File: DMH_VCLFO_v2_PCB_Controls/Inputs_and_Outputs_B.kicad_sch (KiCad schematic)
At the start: 41 parts, among them J13 TS_Jack_6.35mm_Sw, J14 TS_Jack_6.35mm_Sw, J15 TS_Jack_6.35mm_Sw, J16 TS_Jack_6.35mm_Sw, J17 TS_Jack_6.35mm_Sw, J18 TS_Jack_6.35mm_Sw, J29 Conn_01x08, J30 Conn_01x08, J31 IDC_02x05, J32 Conn_01x08, J33 Conn_01x08, Q5 BC548, Q6 BC558, SW10 SPDT_OnOffOn, SW11 SW_SPDT, SW12 SW_SPDT, SW9 SW_SPDT, U3 TL074

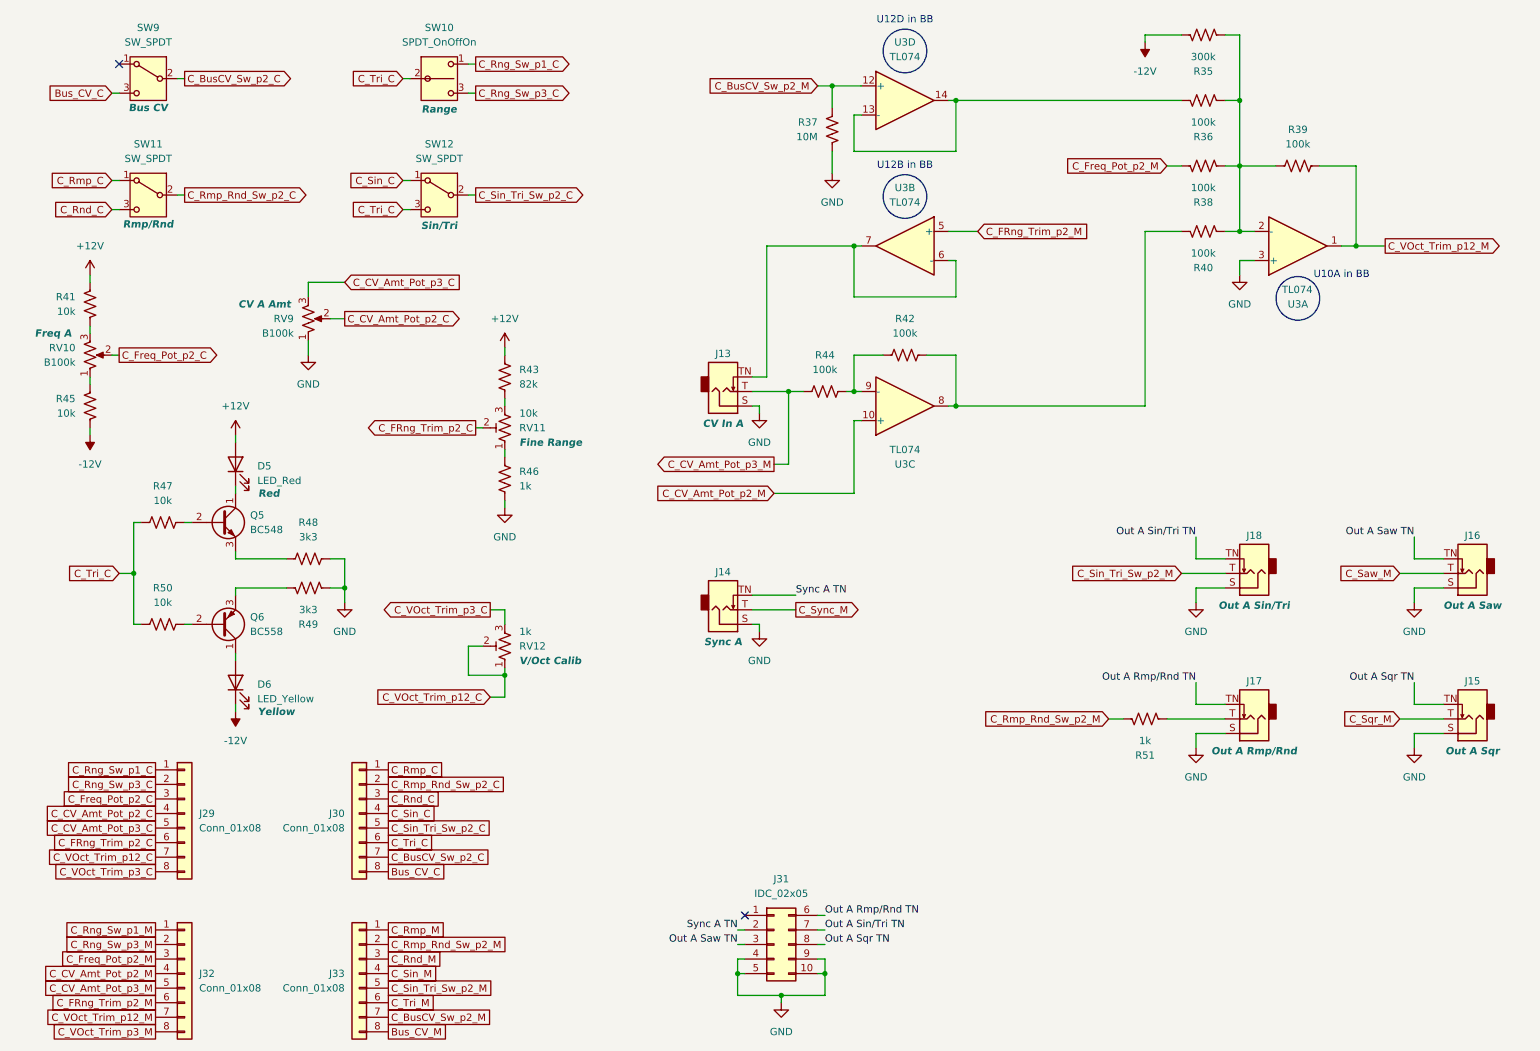
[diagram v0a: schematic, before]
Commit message: Controls PCB comp placement in progress
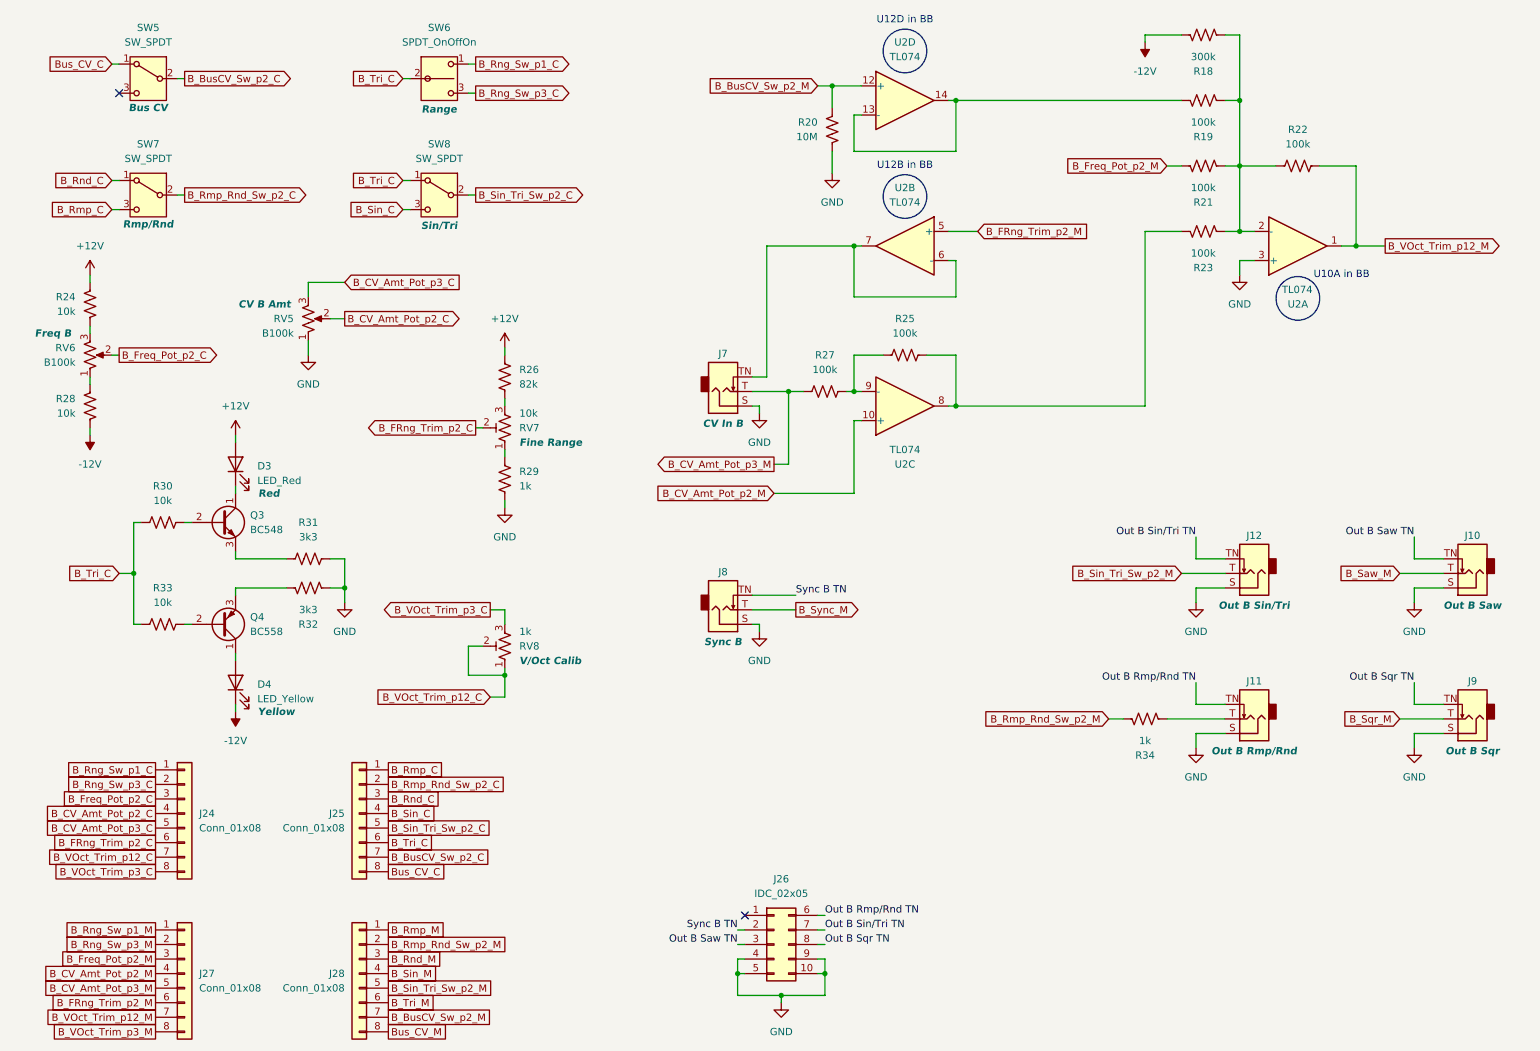
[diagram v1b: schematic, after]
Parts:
- J10: renamed from J16; Function Out A Saw -> Out B Saw
- J11: renamed from J17; Function Out A Rmp/Rnd -> Out B Rmp/Rnd
- J12: renamed from J18; Function Out A Sin/Tri -> Out B Sin/Tri
- J24: renamed from J29; footprint Connector_PinHeader_2.54mm:PinHeader_1x08_P2.54mm_Vertical -> Connector_PinSocket_2.54mm:PinSocket_1x08_P2.54mm_Vertical
- J25: renamed from J30; footprint Connector_PinHeader_2.54mm:PinHeader_1x08_P2.54mm_Vertical -> Connector_PinSocket_2.54mm:PinSocket_1x08_P2.54mm_Vertical
- J7: renamed from J13; Function CV In A -> CV In B
- J8: renamed from J14; Function Sync A -> Sync B
- J9: renamed from J15; Function Out A Sqr -> Out B Sqr
- RV5: renamed from RV9; Function CV A Amt -> CV B Amt
- RV6: renamed from RV10; Function Freq A -> Freq B
- renumbered D5 to D3, D6 to D4, J31 to J26, J32 to J27, J33 to J28, Q5 to Q3, Q6 to Q4, R35 to R18, R36 to R19, R37 to R20, R38 to R21, R39 to R22, R40 to R23, R41 to R24, R42 to R25, R43 to R26, R44 to R27, R45 to R28, R46 to R29, R47 to R30, R48 to R31, R49 to R32, R50 to R33, R51 to R34, RV11 to RV7, RV12 to RV8, SW9 to SW5, SW10 to SW6, SW11 to SW7, SW12 to SW8, U3 to U2
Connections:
- net Bus_CV_C: now also SW5.1 (A); no longer SW5.3 (C)
- net C_BusCV_Sw_p2_C renamed B_BusCV_Sw_p2_C
- net C_BusCV_Sw_p2_M renamed B_BusCV_Sw_p2_M
- net C_CV_Amt_Pot_p2_C renamed B_CV_Amt_Pot_p2_C
- net C_CV_Amt_Pot_p2_M renamed B_CV_Amt_Pot_p2_M
- net C_CV_Amt_Pot_p3_C renamed B_CV_Amt_Pot_p3_C
- net C_CV_Amt_Pot_p3_M renamed B_CV_Amt_Pot_p3_M
- net C_FRng_Trim_p2_C renamed B_FRng_Trim_p2_C
- net C_FRng_Trim_p2_M renamed B_FRng_Trim_p2_M
- net C_Freq_Pot_p2_C renamed B_Freq_Pot_p2_C
- net C_Freq_Pot_p2_M renamed B_Freq_Pot_p2_M
- net C_Rmp_C renamed B_Rmp_C
- net B_Rmp_C: now also SW7.3 (C); no longer SW7.1 (A)
- net C_Rmp_M renamed B_Rmp_M
- net C_Rmp_Rnd_Sw_p2_C renamed B_Rmp_Rnd_Sw_p2_C
- net C_Rmp_Rnd_Sw_p2_M renamed B_Rmp_Rnd_Sw_p2_M
- net C_Rnd_C renamed B_Rnd_C
- net B_Rnd_C: now also SW7.1 (A); no longer SW7.3 (C)
- net C_Rnd_M renamed B_Rnd_M
- net C_Rng_Sw_p1_C renamed B_Rng_Sw_p1_C
- net C_Rng_Sw_p1_M renamed B_Rng_Sw_p1_M
- net C_Rng_Sw_p3_C renamed B_Rng_Sw_p3_C
- net C_Rng_Sw_p3_M renamed B_Rng_Sw_p3_M
- net C_Saw_M renamed B_Saw_M
- net C_Sin_C renamed B_Sin_C
- net B_Sin_C: now also SW8.3 (C); no longer SW8.1 (A)
- net C_Sin_M renamed B_Sin_M
- net C_Sin_Tri_Sw_p2_C renamed B_Sin_Tri_Sw_p2_C
- net C_Sin_Tri_Sw_p2_M renamed B_Sin_Tri_Sw_p2_M
- net C_Sqr_M renamed B_Sqr_M
- net C_Sync_M renamed B_Sync_M
- net C_Tri_C renamed B_Tri_C
- net B_Tri_C: now also SW8.1 (A); no longer SW8.3 (C)
- net C_Tri_M renamed B_Tri_M
- net C_VOct_Trim_p12_C renamed B_VOct_Trim_p12_C
- net C_VOct_Trim_p12_M renamed B_VOct_Trim_p12_M
- net C_VOct_Trim_p3_C renamed B_VOct_Trim_p3_C
- net C_VOct_Trim_p3_M renamed B_VOct_Trim_p3_M
- net Out A Rmp/Rnd TN renamed Out B Rmp/Rnd TN
- net Out A Saw TN renamed Out B Saw TN
- net Out A Sin/Tri TN renamed Out B Sin/Tri TN
- net Out A Sqr TN renamed Out B Sqr TN
- net Sync A TN renamed Sync B TN

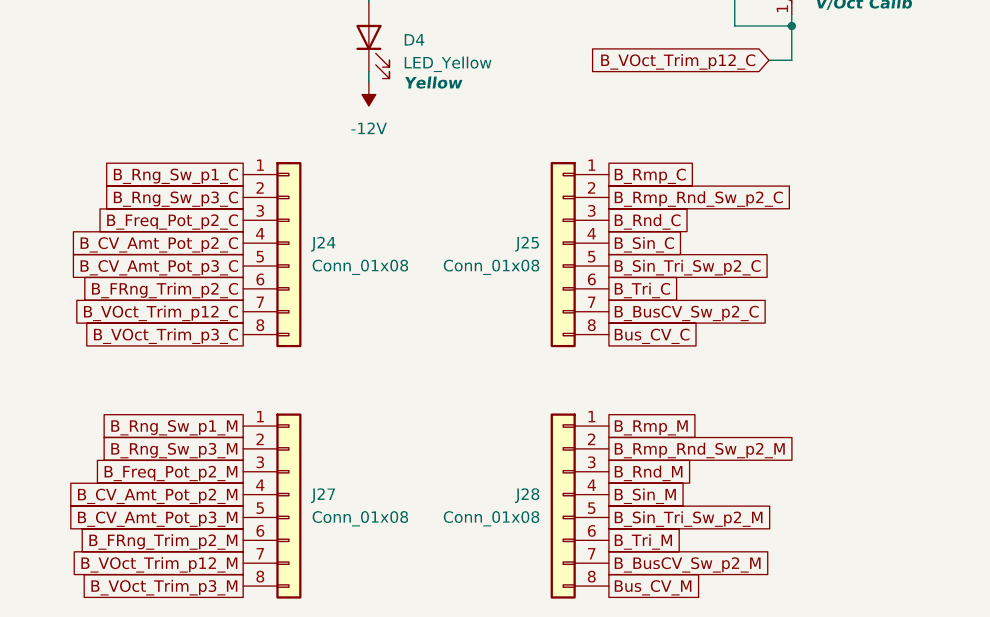
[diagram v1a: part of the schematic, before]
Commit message: Controls PCB routing done
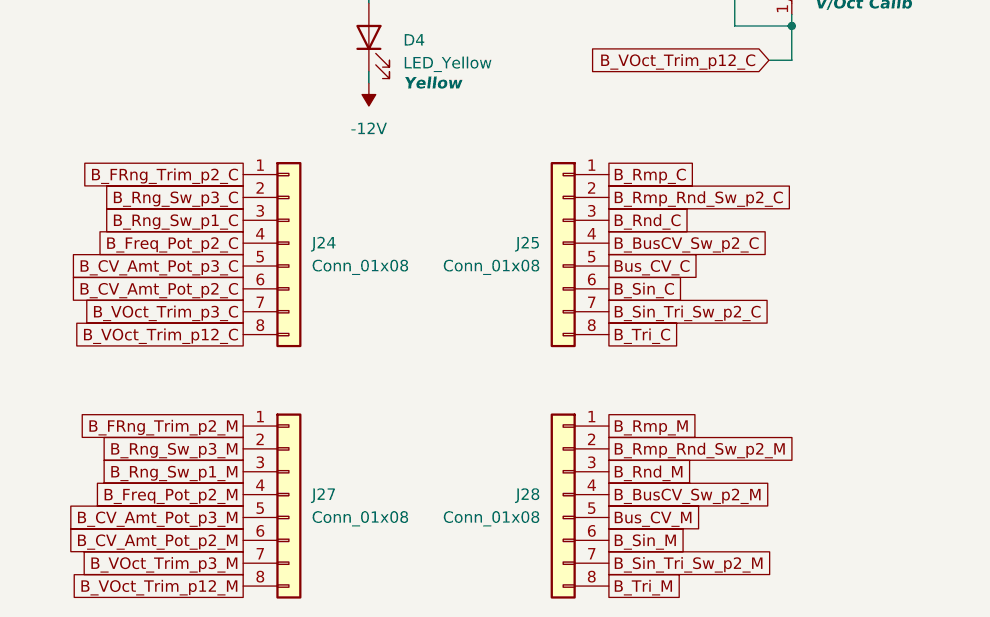
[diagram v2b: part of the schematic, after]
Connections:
- net B_BusCV_Sw_p2_C: now also J25.4 (Pin_4); no longer J25.7 (Pin_7)
- net B_BusCV_Sw_p2_M: now also J28.4 (Pin_4); no longer J28.7 (Pin_7)
- net B_CV_Amt_Pot_p2_C: now also J24.6 (Pin_6); no longer J24.4 (Pin_4)
- net B_CV_Amt_Pot_p2_M: now also J27.6 (Pin_6); no longer J27.4 (Pin_4)
- net B_FRng_Trim_p2_C: now also J24.1 (Pin_1); no longer J24.6 (Pin_6)
- net B_FRng_Trim_p2_M: now also J27.1 (Pin_1); no longer J27.6 (Pin_6)
- net B_Freq_Pot_p2_C: now also J24.4 (Pin_4); no longer J24.3 (Pin_3)
- net B_Freq_Pot_p2_M: now also J27.4 (Pin_4); no longer J27.3 (Pin_3)
- net B_Rng_Sw_p1_C: now also J24.3 (Pin_3); no longer J24.1 (Pin_1)
- net B_Rng_Sw_p1_M: now also J27.3 (Pin_3); no longer J27.1 (Pin_1)
- net B_Sin_C: now also J25.6 (Pin_6); no longer J25.4 (Pin_4)
- net B_Sin_M: now also J28.6 (Pin_6); no longer J28.4 (Pin_4)
- net B_Sin_Tri_Sw_p2_C: now also J25.7 (Pin_7); no longer J25.5 (Pin_5)
- net B_Sin_Tri_Sw_p2_M: now also J28.7 (Pin_7); no longer J28.5 (Pin_5)
- net B_Tri_C: now also J25.8 (Pin_8); no longer J25.6 (Pin_6)
- net B_Tri_M: now also J28.8 (Pin_8); no longer J28.6 (Pin_6)
- net B_VOct_Trim_p12_C: now also J24.8 (Pin_8); no longer J24.7 (Pin_7)
- net B_VOct_Trim_p12_M: now also J27.8 (Pin_8); no longer J27.7 (Pin_7)
- net B_VOct_Trim_p3_C: now also J24.7 (Pin_7); no longer J24.8 (Pin_8)
- net B_VOct_Trim_p3_M: now also J27.7 (Pin_7); no longer J27.8 (Pin_8)
- net Bus_CV_C: now also J25.5 (Pin_5); no longer J25.8 (Pin_8)
- net Bus_CV_M: now also J28.5 (Pin_5); no longer J28.8 (Pin_8)

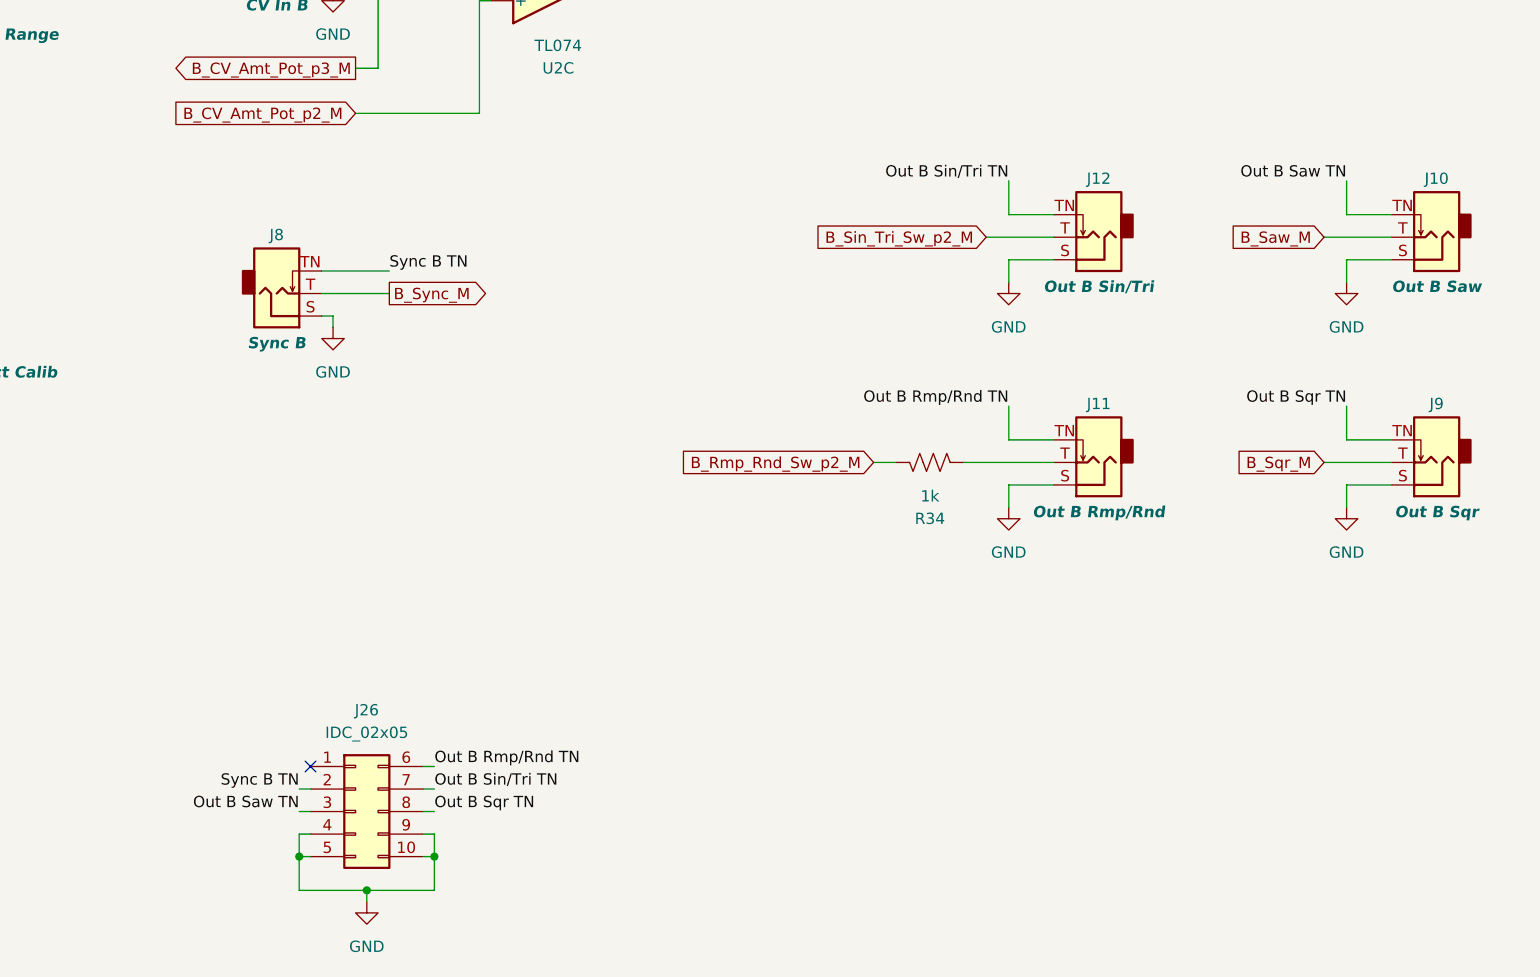
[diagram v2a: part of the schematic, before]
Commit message: Synced Controls PCB with Main
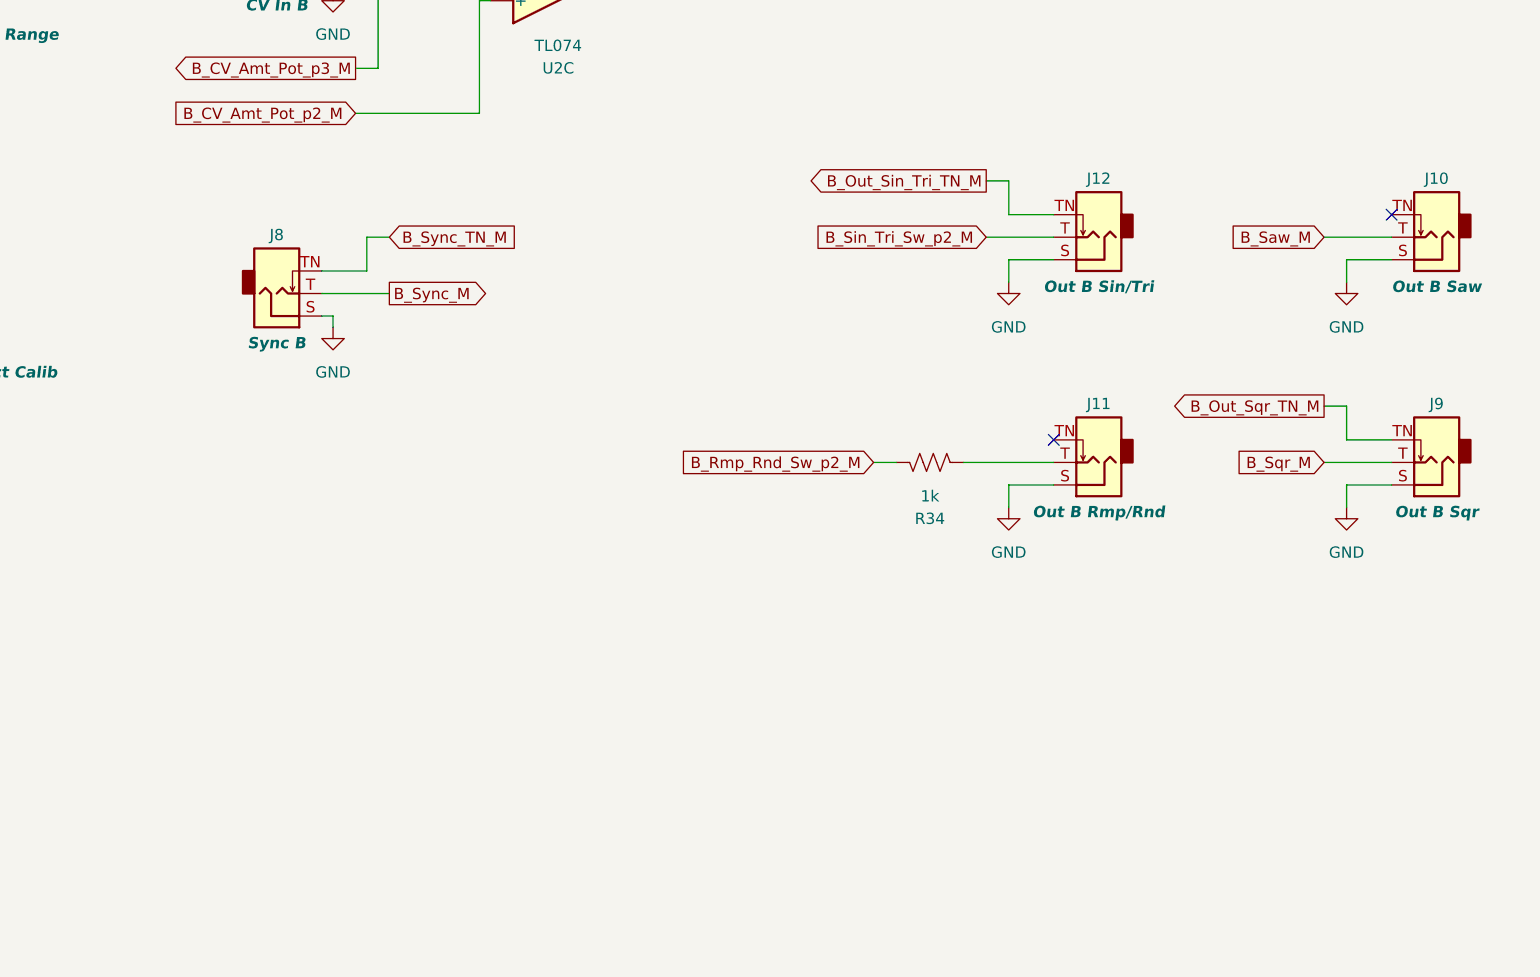
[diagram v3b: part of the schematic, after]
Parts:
- removed J26: IDC_02x05, SynthStuff:IDC-Header_2x05_P2.54mm_Vertical_BackBone, symbol SynthStuff:BackBone_Connector_10Pin
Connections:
- net Out B Rmp/Rnd TN: no longer names the net of J11.TN
- net Out B Saw TN: no longer names the net of J10.TN
- net Out B Sin/Tri TN renamed B_Out_Sin_Tri_TN_M
- net Out B Sqr TN renamed B_Out_Sqr_TN_M
- net Sync B TN renamed B_Sync_TN_M
- no-connect marks 2 -> 3
